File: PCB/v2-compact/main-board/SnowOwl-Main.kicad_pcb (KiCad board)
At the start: 4 copper layers, 70 x 100 mm, 30 parts, among them J1 STACK_2x10, J20 USB-C, J30 microSD, J31 TFT_SPI, SW1 BTN_UP, SW2 BTN_DN, SW3 BTN_L, SW4 BTN_R, SW5 BTN_OK, U20 ESP32-S3-WROOM-1-N8, U21 AP7361C-3.3, U22 USBLC6-2SC6

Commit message: PCB: place the battery + charger power parts on the shield (south back)
Import and place the 24 new power components on the shield's south-back, below the RV1106
and beside the J50 USB-C charge port: BQ25896 charger (U55), TPS63020 buck-boost (U58),
TPS61230A boost (U59), MAX17048 gauge (U57), DW01 protection (U56), AP7361C LDO (U41),
three inductors (L55/58/59), the JST battery connector (BT50), and their passives.

Upgraded the placement anchoring to a SAME-SHEET rule (a support part only anchors to a spec
IC on its own schematic sheet) instead of the single-point distance heuristic - this keeps
each part in its floorplan zone and handles the multi-IC power sheet correctly.

Shield re-verified: 0 same-side overlaps, 0 cross-side hole collisions, 0 parts too close to a
mounting hole, all 105 parts placed. The battery/charger is now physically on the board.
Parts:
- R33, R34: moved to F.Cu
- moved R33 51.4 mm to (37.4, 39.2), turned to 0 degrees
- moved R34 47.2 mm to (88.8, 34.0), turned to 0 degrees

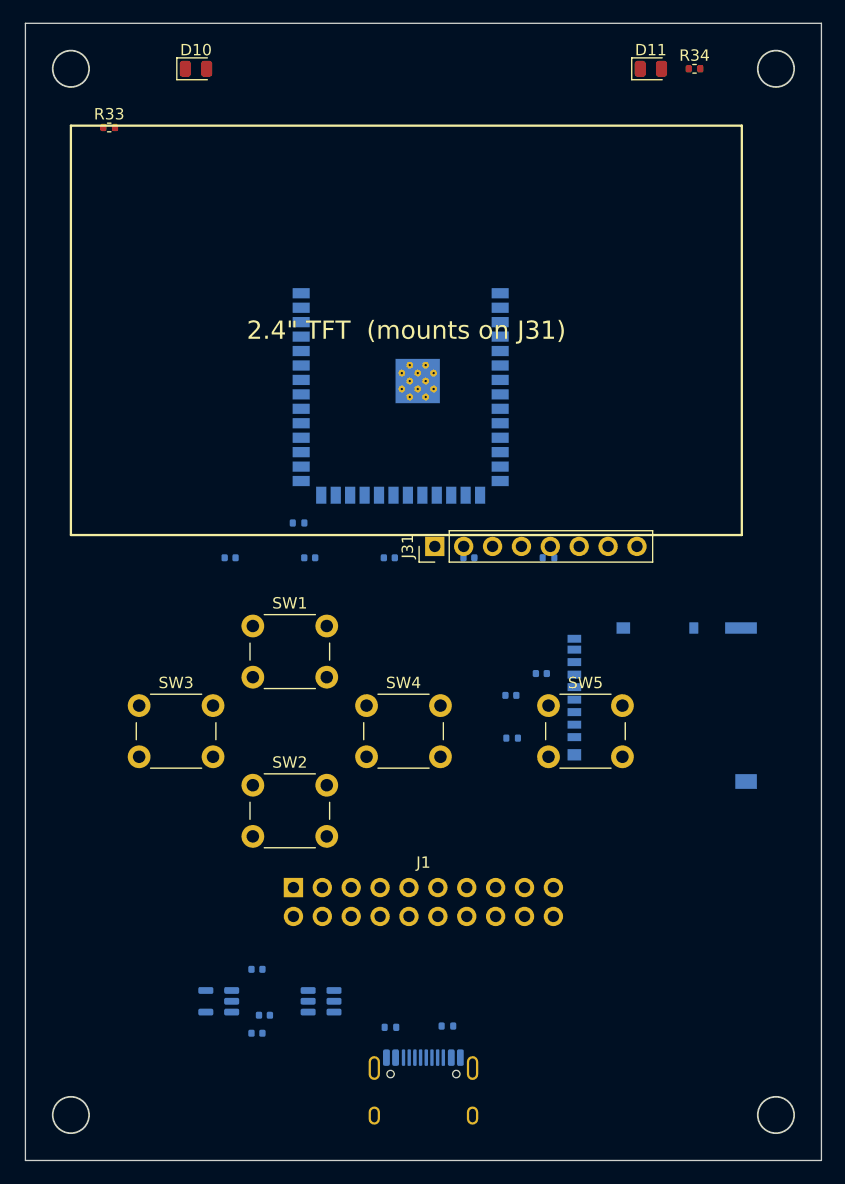
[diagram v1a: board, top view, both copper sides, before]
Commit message: Boards: black solder-mask stackup, GND/3V3 plane pours, ESP32-BlackRaven silkscreen art
- Add a 4-layer stackup with BLACK solder mask to both boards (renders/fab in black).
- Pour the inner reference planes: solid GND on the 'GND' layer and +3V3 on the '3V3' layer,
  both boards (~6500mm2 / ~5500mm2 coverage).
- ESP32-BlackRaven branding on the MAIN front: convert the skeletal-raven line-art and the
  bone-font logo to white F.SilkS polygons (scratchpad/img2silk.py, greedy rectangle decomposition
  since bitmap2component is GUI-only) - raven fills the board (~58x81mm, 2419 polys), logo across
  the bottom by the D-pad. New Art_BlackRaven / Art_Logo footprints in SnowOwl.pretty; injected as
  board text (FootprintLoad chokes on the 2419-poly footprint). Removed the old TFT screen label.
- Main-board power reconciliation (schematic): main is now powered from the shield battery over J1;
  J20 USB-C = S3 data/programming only (VBUS_MAIN, not a supply); redundant main LDO U21 removed.

WIP sync note: the schematic main-power change + the datasheet pinout corrections are NOT yet
re-imported to the .kicad_pcb - that's the next batch (re-import removes U21, folds pinout fixes,
re-fills planes). Silkscreen art currently overlaps some pads (buttons/J1/J31) - fab clips silk off
pads, but a clean pass should mask the art away from pads.
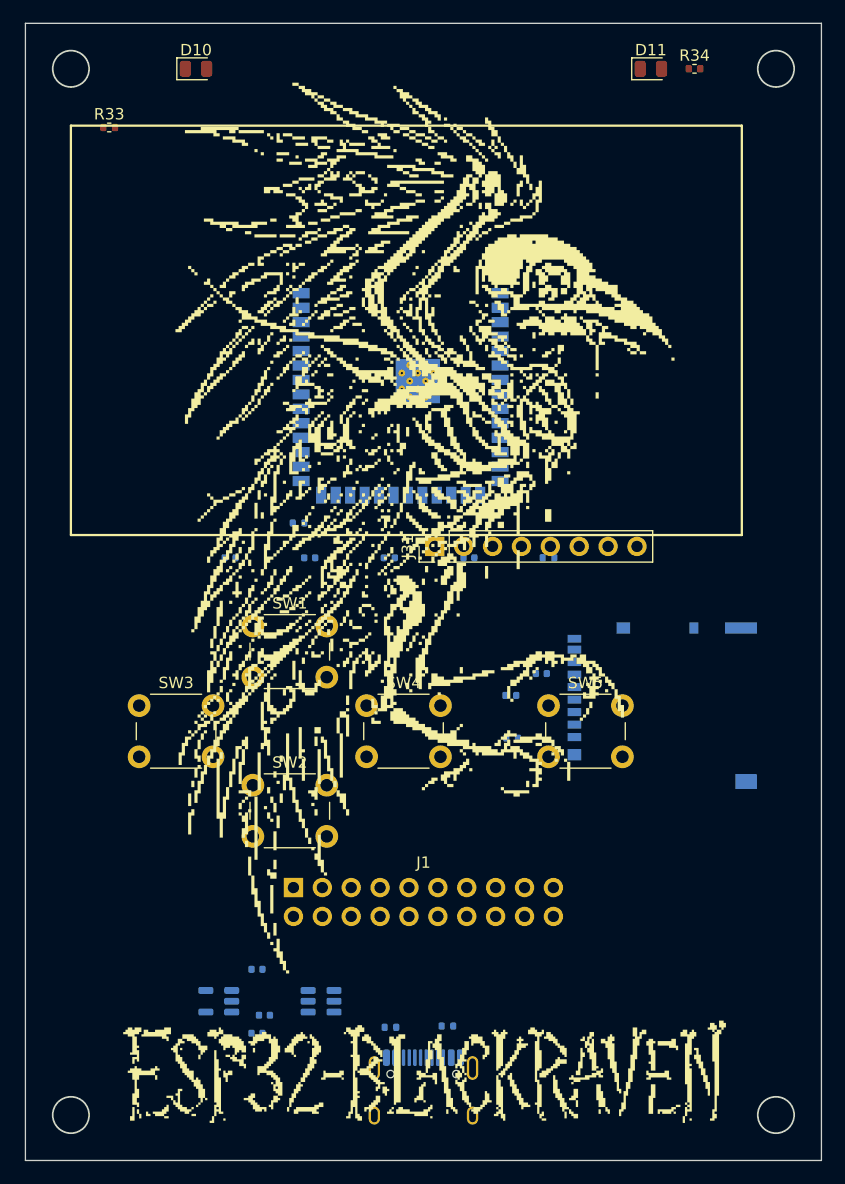
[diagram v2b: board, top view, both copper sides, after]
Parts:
- added ?: , Art_Logo, F.Cu at (65.0, 121.0)
- added ?: , Art_BlackRaven, F.Cu at (65.0, 73.0)
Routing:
- added copper zone on In2.Cu, net +3V3
- added copper zone on In1.Cu, net GND
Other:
- board text removed: "2.4" TFT (mounts on J31)"

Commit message: Single USB-C + battery power; J1 vertical on the left edge; U30 model; back-side comments
Power/architecture:
- Remove J50 (the RV1106's own USB-C). The device now has ONE USB-C: the main board's J20.
  J20's VBUS is carried over J1 pin19 (was SPARE) to the shield's BQ25896 charger, so charging +
  the ESP32-S3 data/programming share the single port. Everything runs off the battery.
- Reconcile the nets: J20 VBUS -> VBUS (was VBUS_MAIN), charger VBUS <- J1 pin19, RV1106 keeps its
  microSD (J51) but loses its USB port (reached over UART on J1). Removed orphans R95/R96 (J50 CC
  resistors) and the redundant main LDO U21. Verified: J1 mates 20/20 on both boards, VBUS spans
  J20 -> J1 -> U55, GND healthy (106/37 nodes), no bad net merges.

Placement:
- J1 stack header: was horizontal mid-board, now VERTICAL on the WEST edge at the same spot on both
  boards (they still mate). Nudged the shield's PN532/flash/HTRC (U7/U12/U8) east to clear it, and
  the main's screen east. Status LEDs D10/D11 pulled off the corner mounting holes. 0 real overlaps.

3D + silk:
- U30 (RV1106 Core1106): no KiCad model exists for the Luckfox SoM -> add a sized VRML module
  stand-in (SnowOwl.3dshapes/RV1106_Core1106.wrl; sizes pre-divided by 2.54 for KiCad's inch-unit
  VRML reader). USB-C model: swap the vertical USB4085 for the 16-pin horizontal USB4105 so it
  seats correctly against the horizontal HRO footprint.
- ESP32-BlackRaven art: logo moved to the top by the LEDs, raven dropped down to fill the board.
  Dropped the cluttering TFT label (fab outline kept). Added five back-side silkscreen comments on
  the main board (title/rev, battery, power path, USB-C role, J1 purpose).

Deferred (SWIG pcbnew geometry calls are failing in this environment right now): re-pour the inner
GND/+3V3 planes (inner layers, not visible in renders); apply the datasheet pinout/value fixes to
the power ICs (BQ25896/TPS63020/TPS61230A/MAX17048).
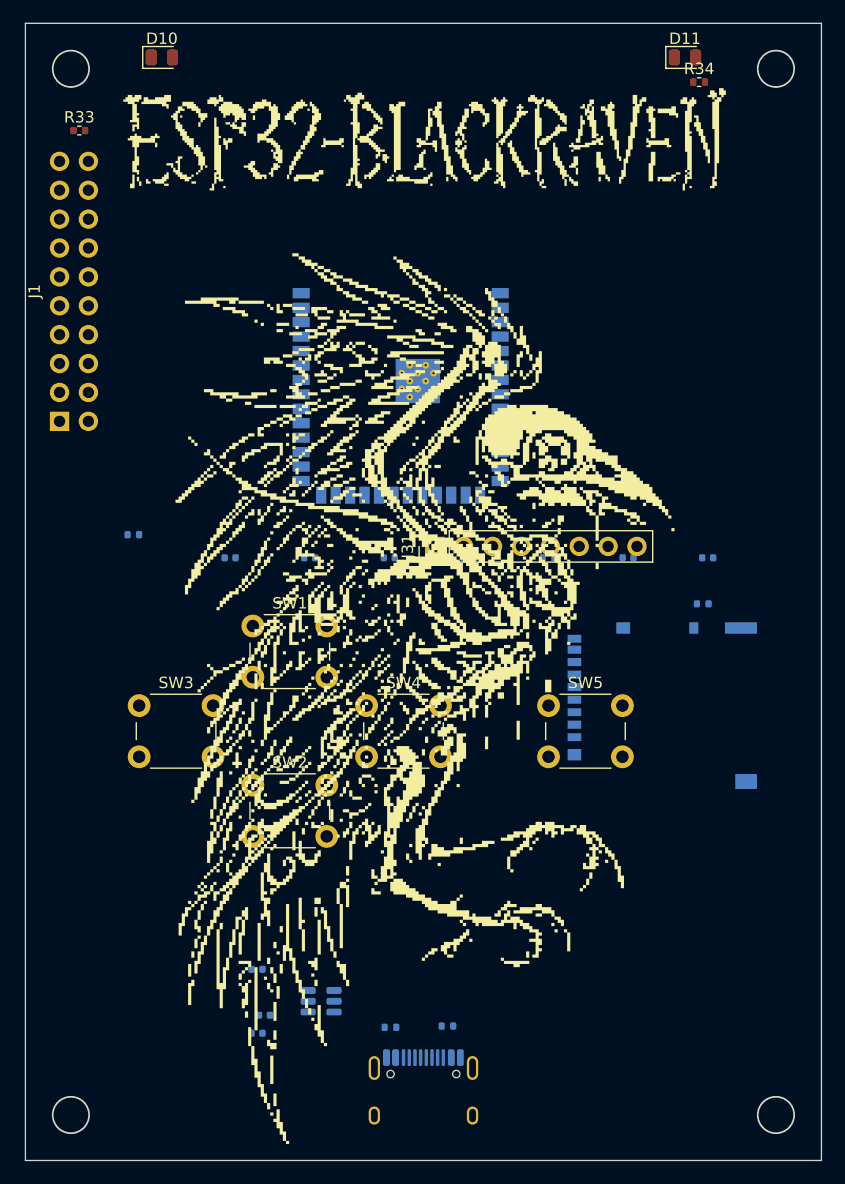
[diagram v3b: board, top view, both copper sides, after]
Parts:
- removed U21: AP7361C-3.3, SOT-23-5
- ? (x2): moved to F.SilkS
- moved ? 82.0 mm to (65.0, 39.0)
- moved J1 45.9 mm to (33.0, 65.0), turned to 90 degrees
- moved C35 21.1 mm to (90.0, 77.0)
- moved R32 20.5 mm to (89.6, 81.0)
- moved ? 15.0 mm to (65.0, 88.0)
- moved R31 14.6 mm to (39.5, 75.0)
- moved C34 12.7 mm to (83.0, 77.0)
- moved D10 3.16 mm to (42.0, 33.0)
- moved D11 3.16 mm to (88.0, 33.0)
- moved R33 2.64 mm to (34.7, 39.4)
- moved R34 1.24 mm to (89.2, 35.2)
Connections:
- J1 pad 19: SPARE -> VBUS
- J20 pad A4: +5V -> VBUS
- J20 pad A9: +5V -> VBUS
- J20 pad B4: +5V -> VBUS
- J20 pad B9: +5V -> VBUS
- U22 pad 5: +5V -> VBUS
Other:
- board text added: "ESP32-BLACKRAVEN - MAIN rev.A"
- board text added: "J1 stack: power + I2C + UART"
- board text added: "Li-Po charges via USB-C ~2500mAh 1-2 h"
- board text added: "Powered from shield battery over J1 (+5V/+3V3)"
- board text added: "USB-C J20: charge + ESP32-S3 data/flash"
